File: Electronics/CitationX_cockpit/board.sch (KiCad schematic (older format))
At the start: 40 parts

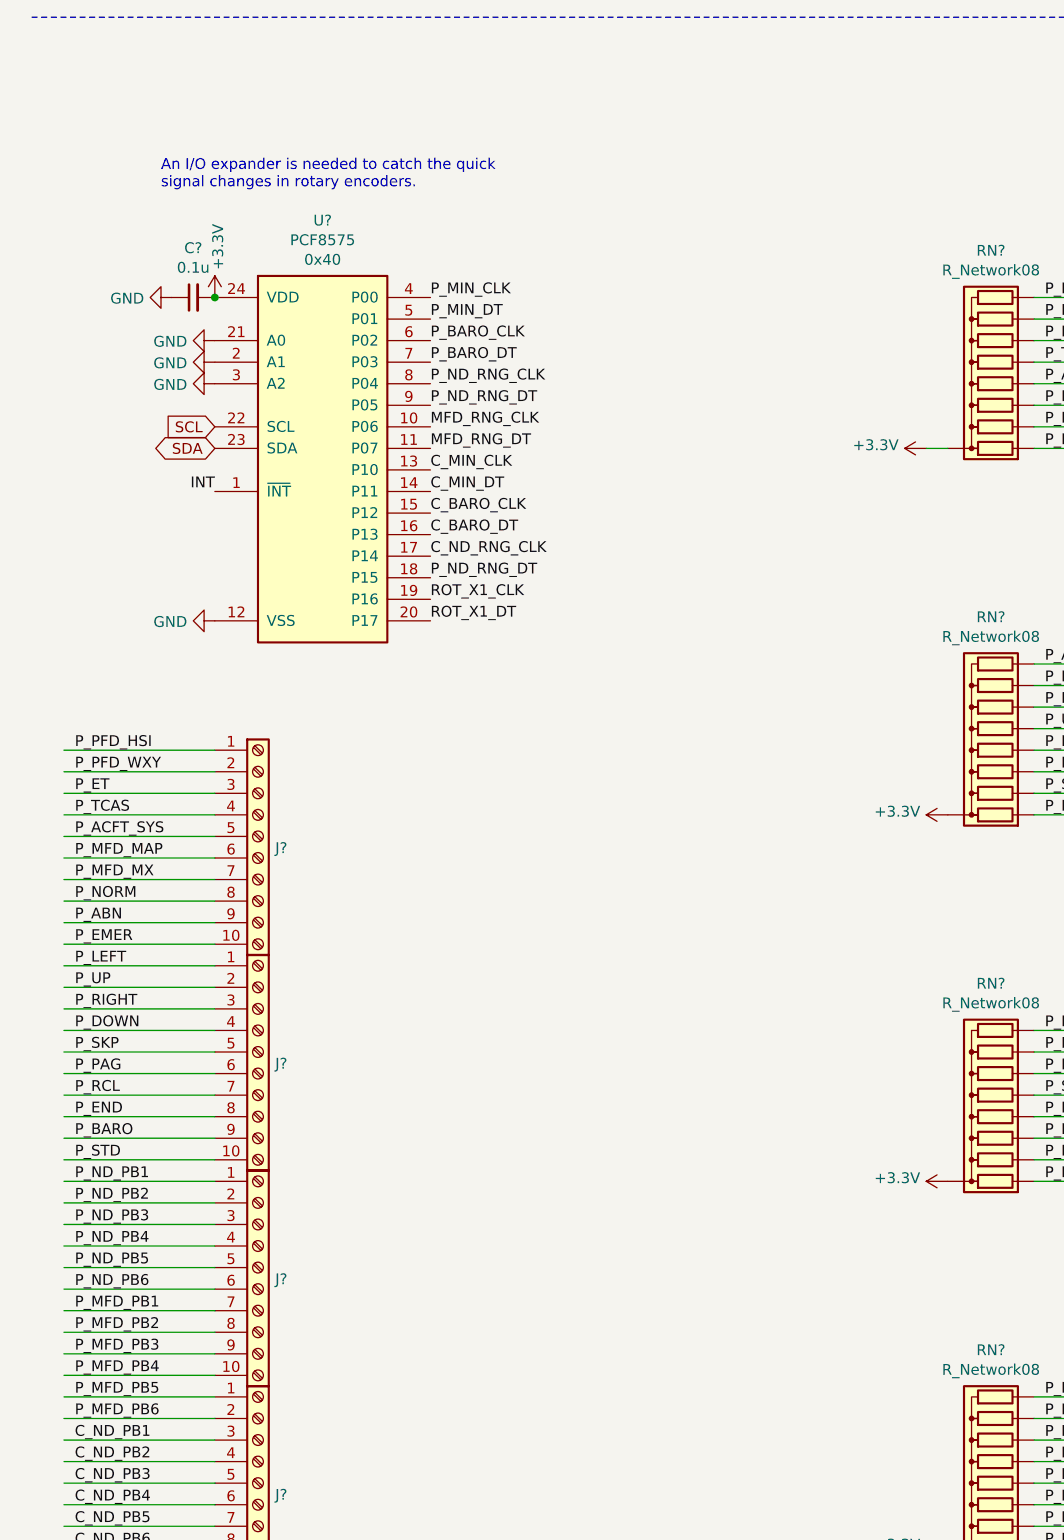
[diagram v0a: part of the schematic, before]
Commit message: Electronics - Working on copilot side and APU
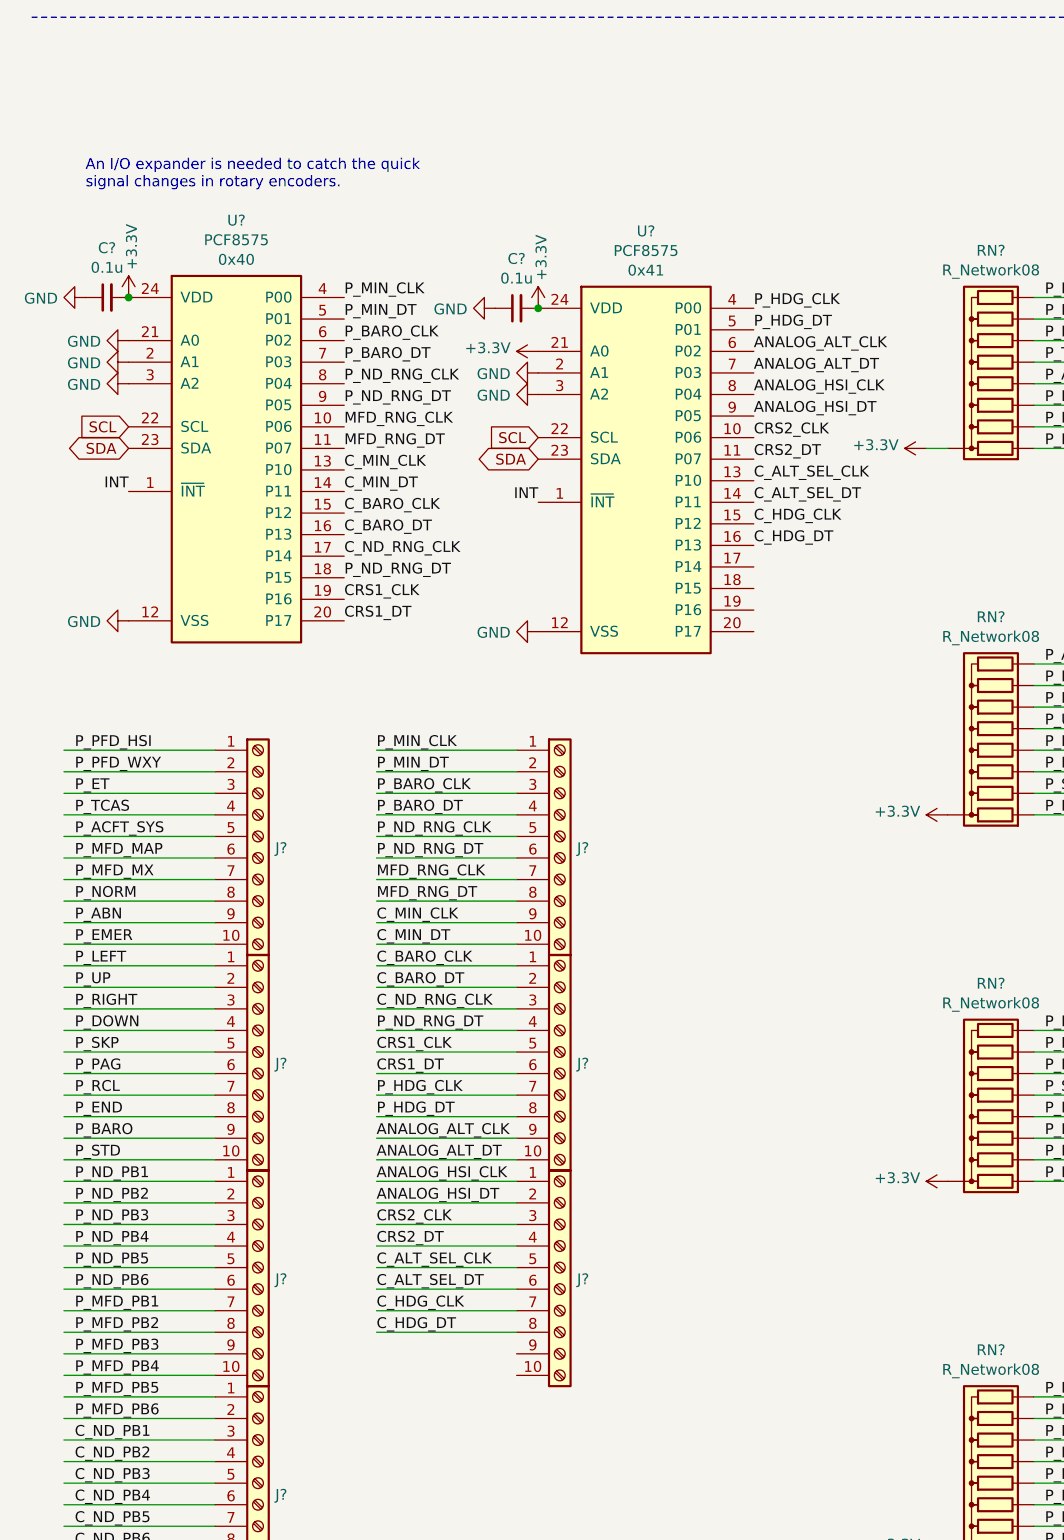
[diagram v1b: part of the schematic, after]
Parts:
- added C?: 0.1u, symbol Device:C_Small
- added J? (x3): Screw_Terminal_01x10, symbol Connector:Screw_Terminal_01x10
- added U?: PCF8575, IPC7351-Nominal:SOP65P775X200-24, symbol NXP:PCF8575
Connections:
- net labels added: ANALOG_ALT_CLK, ANALOG_ALT_DT, ANALOG_HSI_CLK, ANALOG_HSI_DT, CRS1_CLK, CRS1_DT, CRS2_CLK, CRS2_DT, C_ALT_SEL_CLK, C_ALT_SEL_DT, C_HDG_CLK, C_HDG_DT, P_HDG_CLK, P_HDG_DT
- net labels removed: ROT_X1_CLK, ROT_X1_DT
- wire segments 175 -> 203
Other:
- moved on the sheet: C?, U?

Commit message: Electronics - Misc. works
Continued (and checked board). All connections are probably OK.
Fixed hierarchical pins in APUs (affects all schematics)
Numbered elements for testing schematics
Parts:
- removed C? (x3): 0.1u, symbol Device:C_Small
- removed J? (x8): Screw_Terminal_01x10, symbol Connector:Screw_Terminal_01x10
- removed RN? (x3): R_Network08, Resistor_THT:R_Array_SIP9, symbol Device:R_Network08
- removed U? (x3): 74HC165, symbol pkl_misc:74HC165
- added C26, C28, C36, C37, C38: 0.1u, symbol Device:C_Small
- added J17, J18, J19, J20, J21, J22, J23, J24, J25: Screw_Terminal_01x10, symbol Connector:Screw_Terminal_01x10
- added RN11, RN12, RN13: R_Network08, Resistor_THT:R_Array_SIP9, symbol Device:R_Network08
- added U18: PCF8575, IPC7351-Nominal:SOP65P775X200-24, symbol NXP:PCF8575
- added U20: 74HC595, symbol 74xx:74HC595
- added U28, U29, U30: 74HC165, symbol pkl_misc:74HC165
- gave numbers to parts that had none: 28
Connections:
- net labels added: C_BARO_PB, C_BRG_L_ADF1, C_BRG_L_FMS1, C_BRG_L_OFF, C_BRG_L_VOR1, C_BRG_R_ADF2, C_BRG_R_FMS2, C_BRG_R_OFF, C_BRG_R_VOR2, C_CRS2_CLK, C_CRS2_DT, C_CRS2_PB, C_DAU1_REV_PB, C_DAU2_REV_PB, C_ED_L, C_ED_R, C_FMS_PB, C_HDG_PB, C_MC_RESET_LED, C_MC_RESET_PB, C_MW_RESET_LED, C_MW_RESET_PB, C_NAV_PB, C_ND_RNG_DT, C_PREV_PB, C_SG_REV_SG1, C_SG_REV_SG2, C_STD_PB, C_VHF_CLK, C_VHF_COM_LED, C_VHF_DT, C_VHF_NAV, C_VHF_NAV_LED, C_VHF_PB, C_VHF_PB1, C_VHF_PB2, C_VHF_PB3, MFD_PB1, MFD_PB2, MFD_PB3, MFD_PB4, MFD_PB5, MFD_PB6, OSR_IN, OSR_LATCH, OSR_OUT, P_BARO_PB, P_BRG_L_ADF1, P_BRG_L_FMS1, P_BRG_L_OFF, P_BRG_L_VOR1, P_BRG_R_ADF2, P_BRG_R_FMS2, P_BRG_R_OFF, P_BRG_R_VOR2, P_CRS1_CLK, P_CRS1_DT, P_CRS1_PB, P_FMS_PB, P_HDG_PB, P_MC_RESET_LED, P_MC_RESET_PB, P_MW_RESET_LED, P_MW_RESET_PB, P_NAV_PB, P_ND_CLK, P_ND_DT, P_PREV_PB, P_STB_ALT_CLK, P_STB_ALT_DT, P_STD_PB, STB_HSI_CLK, STB_HSI_DT
- net labels removed: ANALOG_ALT_CLK, ANALOG_ALT_DT, ANALOG_HSI_CLK, ANALOG_HSI_DT, CRS1_CLK, CRS1_DT, CRS2_CLK, CRS2_DT, C_ABN, C_ACFT_SYS, C_DOWN, C_EMER, C_END, C_ET, C_LEFT, C_MFD_MAP, C_MFD_MX, C_NORM, C_PAG, C_PFD_HSI, C_PFD_WXY, C_RCL, C_RIGHT, C_SKP, C_STD, C_TCAS, C_UP, ISR_X1, ISR_X2, ISR_X3, ISR_X4, ISR_X5, ISR_X6, ISR_X7, P_ABN, P_ACFT_SYS, P_BARO, P_DOWN, P_EMER, P_END, P_ET, P_LEFT, P_MFD_MAP, P_MFD_MX, P_MFD_PB1, P_MFD_PB2, P_MFD_PB3, P_MFD_PB4, P_MFD_PB5, P_MFD_PB6, P_ND_RNG_CLK, P_ND_RNG_DT, P_NORM, P_PAG, P_PFD_HSI, P_PFD_WXY, P_RCL, P_RIGHT, P_SKP, P_STD, P_TCAS, P_UP
- wire segments 203 -> 117
- no-connect marks 22 -> 37
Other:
- note added: "Todo : check all wires in screw terminal anc make sure they exist in I/O shift registers"
- moved on the sheet: C27, J16, U19

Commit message: Electronics - Misc works
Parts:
- added J?: Screw_Terminal_01x02, symbol Connector:Screw_Terminal_01x02
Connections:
- net AP_NOSE_CLK: now reaches U18.8 (P04)
- net AP_NOSE_CLK: now also J?.1 (Pin_1)
- net AP_NOSE_DT: now reaches U18.9 (P05)
- net AP_NOSE_DT: now also J?.2 (Pin_2)
- no-connect marks 37 -> 35
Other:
- note removed: "Todo : check all wires in screw terminal anc make sure they exist in I/O shift registers"
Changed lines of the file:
@@
 Text Label 1750 6800 0    50   ~ 0
 P_MW_RESET_PB
-Text Notes 7250 15000 0    50   ~ 0
-Todo : check all wires in screw terminal anc make sure they exist in I/O shift registers
 Text Label 1750 7100 0    50   ~ 0
 P_BRG_L_OFF
@@
 	1    0    0    -1
 $EndComp
-Connection ~ 2950 6050
 $Comp
 L power:GND #PWR?
@@
 NoConn ~ 3900 9150
 NoConn ~ 1950 5500
-NoConn ~ 3950 6450
-NoConn ~ 3950 6550
 NoConn ~ 3950 6650
 NoConn ~ 3950 6750
@@
 Text HLabel 3100 8950 0    50   Input ~ 0
 OSR_LATCH
+$Comp
+L Connector:Screw_Terminal_01x02 J?
+U 1 1 5DDEDB63
+P 3500 15750
+AR Path="/5DC33C09/5DDEDB63" Ref="J?"  Part="1"
+AR Path="/5DB6029E/5DDEDB63" Ref="J?"  Part="1"
+F 0 "J?" H 3580 15742 50  0000 L CNN
+F 1 "Screw_Terminal_01x02" H 3580 15651 50  0000 L CNN
+F 2 "" H 3500 15750 50  0001 C CNN
+F 3 "~" H 3500 15750 50  0001 C CNN
+	1    3500 15750
+	1    0    0    -1
+$EndComp
+Connection ~ 2950 6050
+Text Label 3950 6550 0    50   ~ 0
+AP_NOSE_DT
+Text Label 3950 6450 0    50   ~ 0
+AP_NOSE_CLK
+Wire Wire Line
+	3300 15850 2750 15850
+Text Label 2750 15850 0    50   ~ 0
+AP_NOSE_DT
+Wire Wire Line
+	3300 15750 2750 15750
+Text Label 2750 15750 0    50   ~ 0
+AP_NOSE_CLK
 $EndSCHEMATC

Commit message: Electronics - Misc works
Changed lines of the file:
@@
 EESchema Schematic File Version 4
 LIBS:CitationX_cockpit-cache
-EELAYER 30 0
+EELAYER 26 0
 EELAYER END
 $Descr A3 11693 16535 portrait
@@
 	0    1    1    0
 $EndComp
-Text Label 950  4900 2    50   ~ 0
-INT
 $Comp
 L power:GND #PWR0197
@@
 	0    1    1    0
 $EndComp
-Text Label 3000 4950 2    50   ~ 0
-INT
 $Comp
 L power:GND #PWR?
@@
 	0    1    1    0
 $EndComp
-Text Label 2950 6950 2    50   ~ 0
-INT
 $Comp
 L power:GND #PWR?
@@
 NoConn ~ 3950 7450
 NoConn ~ 3950 7550
-Text HLabel 3100 8950 0    50   Input ~ 0
-OSR_LATCH
 $Comp
 L Connector:Screw_Terminal_01x02 J?
@@
 Text Label 2750 15750 0    50   ~ 0
 AP_NOSE_CLK
+Text GLabel 950  4900 0    50   Output ~ 0
+INT
+Text GLabel 3000 4950 0    50   Output ~ 0
+INT
+Text GLabel 2950 6950 0    50   Output ~ 0
+INT
+Text GLabel 3100 8950 0    50   Input ~ 0
+OSR_LATCH
 $EndSCHEMATC
